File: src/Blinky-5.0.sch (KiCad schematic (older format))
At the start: 7 parts, among them U1 7555

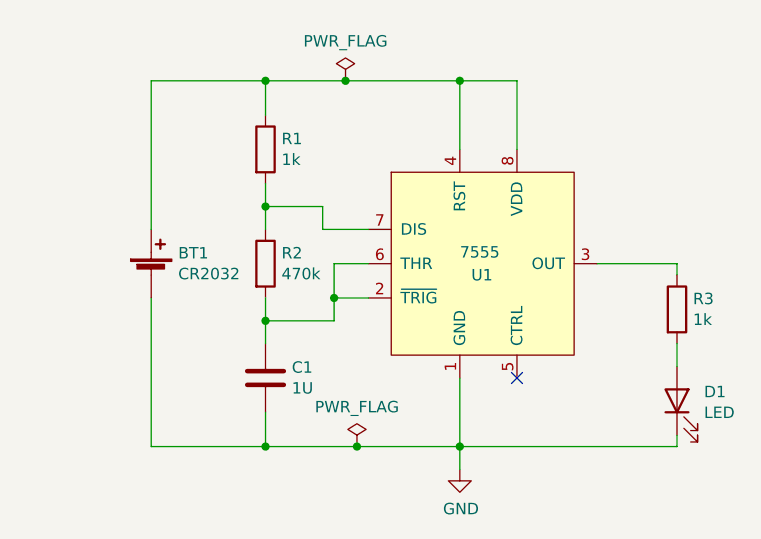
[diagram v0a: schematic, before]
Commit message: Add custom library and additions
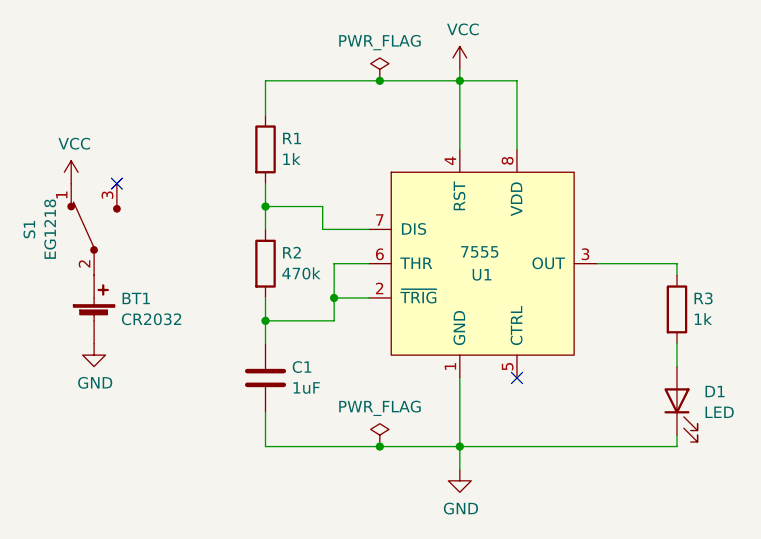
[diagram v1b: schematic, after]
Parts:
- added S1: EG1218, digikey-footprints:Switch_Slide_11.6x4mm_EG1218, symbol dk_Slide-Switches:EG1218
- C1: value 1U -> 1uF
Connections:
- net VCC: now reaches R1.1, U1.4 (RST), U1.8 (VDD)
- net VCC: now also S1.1; no longer BT1.1 (+)
- new net: BT1.1 (+), S1.2
- no-connect marks 1 -> 2
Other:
- moved on the sheet: BT1
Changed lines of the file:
@@
 $EndDescr
-$Comp
-L GTB5:7555 U1
-U 1 1 60908F50
-P 5500 3800
-F 0 "U1" H 5450 3750 50  0000 L CNN
-F 1 "7555" H 5400 3850 50  0000 L CNN
-F 2 "" H 5500 3800 50  0001 C CNN
-F 3 "" H 5500 3800 50  0001 C CNN
-	1    5500 3800
-	1    0    0    -1
-$EndComp
 $Comp
 L Device:R R3
@@
 L Device:Battery_Cell BT1
 U 1 1 6090E03A
-P 4050 3850
-F 0 "BT1" H 4168 3946 50  0000 L CNN
-F 1 "CR2032" H 4168 3855 50  0000 L CNN
-F 2 "" V 4050 3910 50  0001 C CNN
-F 3 "~" V 4050 3910 50  0001 C CNN
-	1    4050 3850
-	1    0    0    -1
-$EndComp
-$Comp
-L power:GND #PWR0101
-U 1 1 6090EEEC
-P 5400 4700
-F 0 "#PWR0101" H 5400 4450 50  0001 C CNN
-F 1 "GND" H 5405 4527 50  0000 C CNN
-F 2 "" H 5400 4700 50  0001 C CNN
-F 3 "" H 5400 4700 50  0001 C CNN
-	1    5400 4700
-	1    0    0    -1
-$EndComp
-Wire Wire Line
-	5650 3000 5650 3300
-Wire Wire Line
-	5400 3300 5400 3000
-Connection ~ 5400 3000
-Wire Wire Line
-	5400 3000 5650 3000
+P 3800 4050
+F 0 "BT1" H 3918 4146 50  0000 L CNN
+F 1 "CR2032" H 3918 4055 50  0000 L CNN
+F 2 "" V 3800 4110 50  0001 C CNN
+F 3 "~" V 3800 4110 50  0001 C CNN
+	1    3800 4050
+	1    0    0    -1
+$EndComp
 $Comp
 L Device:C C1
@@
 P 4550 4300
 F 0 "C1" H 4665 4346 50  0000 L CNN
-F 1 "1U" H 4665 4255 50  0000 L CNN
+F 1 "1uF" H 4665 4255 50  0000 L CNN
 F 2 "" H 4588 4150 50  0001 C CNN
 F 3 "~" H 4550 4300 50  0001 C CNN
@@
 $EndComp
 Wire Wire Line
-	4550 3150 4550 3000
-Connection ~ 4550 3000
-Wire Wire Line
-	4550 3000 4900 3000
-Wire Wire Line
 	4550 3650 4550 3550
 Wire Wire Line
@@
 Wire Wire Line
 	4550 4450 4550 4600
-Connection ~ 4550 4600
+Connection ~ 5400 4600
+Wire Wire Line
+	5400 4600 6350 4600
+Wire Wire Line
+	5400 4600 5400 4300
+NoConn ~ 5650 4300
+$Comp
+L power:VCC #PWR0101
+U 1 1 609267B7
+P 3700 3450
+F 0 "#PWR0101" H 3700 3300 50  0001 C CNN
+F 1 "VCC" H 3715 3623 50  0000 C CNN
+F 2 "" H 3700 3450 50  0001 C CNN
+F 3 "" H 3700 3450 50  0001 C CNN
+	1    3700 3450
+	1    0    0    -1
+$EndComp
+$Comp
+L power:GND #PWR0102
+U 1 1 60927759
+P 3800 4150
+F 0 "#PWR0102" H 3800 3900 50  0001 C CNN
+F 1 "GND" H 3805 3977 50  0000 C CNN
+F 2 "" H 3800 4150 50  0001 C CNN
+F 3 "" H 3800 4150 50  0001 C CNN
+	1    3800 4150
+	1    0    0    -1
+$EndComp
+$Comp
+L power:VCC #PWR0103
+U 1 1 609313FA
+P 5400 2950
+F 0 "#PWR0103" H 5400 2800 50  0001 C CNN
+F 1 "VCC" H 5415 3123 50  0000 C CNN
+F 2 "" H 5400 2950 50  0001 C CNN
+F 3 "" H 5400 2950 50  0001 C CNN
+	1    5400 2950
+	1    0    0    -1
+$EndComp
+$Comp
+L GTB5:7555 U1
+U 1 1 60908F50
+P 5500 3800
+F 0 "U1" H 5450 3750 50  0000 L CNN
+F 1 "7555" H 5400 3850 50  0000 L CNN
+F 2 "" H 5500 3800 50  0001 C CNN
+F 3 "" H 5500 3800 50  0001 C CNN
+	1    5500 3800
+	1    0    0    -1
+$EndComp
+Wire Wire Line
+	5400 3300 5400 3000
+Wire Wire Line
+	4550 3150 4550 3000
+Wire Wire Line
+	4550 3000 5050 3000
+Connection ~ 5400 3000
+Wire Wire Line
+	5650 3300 5650 3000
+Wire Wire Line
+	5650 3000 5400 3000
+Wire Wire Line
+	4550 4600 5050 4600
+Wire Wire Line
+	5400 3000 5400 2950
+$Comp
+L power:GND #PWR0104
+U 1 1 6093A498
+P 5400 4700
+F 0 "#PWR0104" H 5400 4450 50  0001 C CNN
+F 1 "GND" H 5405 4527 50  0000 C CNN
+F 2 "" H 5400 4700 50  0001 C CNN
+F 3 "" H 5400 4700 50  0001 C CNN
+	1    5400 4700
+	1    0    0    -1
+$EndComp
 Wire Wire Line
 	5400 4600 5400 4700
-Wire Wire Line
-	4550 4600 4950 4600
-Connection ~ 5400 4600
-Wire Wire Line
-	5400 4600 6350 4600
-Wire Wire Line
-	5400 4600 5400 4300
-Wire Wire Line
-	4050 3950 4050 4600
-Wire Wire Line
-	4050 4600 4550 4600
-Wire Wire Line
-	4050 3650 4050 3000
-Wire Wire Line
-	4050 3000 4550 3000
 $Comp
 L power:PWR_FLAG #FLG0101
-U 1 1 6091C652
-P 4900 3000
-F 0 "#FLG0101" H 4900 3075 50  0001 C CNN
-F 1 "PWR_FLAG" H 4900 3173 50  0000 C CNN
-F 2 "" H 4900 3000 50  0001 C CNN
-F 3 "~" H 4900 3000 50  0001 C CNN
-	1    4900 3000
-	1    0    0    -1
-$EndComp
-Connection ~ 4900 3000
-Wire Wire Line
-	4900 3000 5400 3000
+U 1 1 6093C855
+P 5050 3000
+F 0 "#FLG0101" H 5050 3075 50  0001 C CNN
+F 1 "PWR_FLAG" H 5050 3173 50  0000 C CNN
+F 2 "" H 5050 3000 50  0001 C CNN
+F 3 "~" H 5050 3000 50  0001 C CNN
+	1    5050 3000
+	1    0    0    -1
+$EndComp
+Connection ~ 5050 3000
+Wire Wire Line
+	5050 3000 5400 3000
 $Comp
 L power:PWR_FLAG #FLG0102
-U 1 1 6091C7F0
-P 4950 4600
-F 0 "#FLG0102" H 4950 4675 50  0001 C CNN
-F 1 "PWR_FLAG" H 4950 4773 50  0000 C CNN
-F 2 "" H 4950 4600 50  0001 C CNN
-F 3 "~" H 4950 4600 50  0001 C CNN
-	1    4950 4600
-	1    0    0    -1
-$EndComp
-Connection ~ 4950 4600
-Wire Wire Line
-	4950 4600 5400 4600
-NoConn ~ 5650 4300
+U 1 1 6093DBDA
+P 5050 4600
+F 0 "#FLG0102" H 5050 4675 50  0001 C CNN
+F 1 "PWR_FLAG" H 5050 4773 50  0000 C CNN
+F 2 "" H 5050 4600 50  0001 C CNN
+F 3 "~" H 5050 4600 50  0001 C CNN
+	1    5050 4600
+	1    0    0    -1
+$EndComp
+Connection ~ 5050 4600
+Wire Wire Line
+	5050 4600 5400 4600
+$Comp
+L dk_Slide-Switches:EG1218 S1
+U 1 1 609476D4
+P 3800 3650
+F 0 "S1" H 3800 3931 50  0000 C CNN
+F 1 "EG1218" H 3800 3840 50  0000 C CNN
+F 2 "digikey-footprints:Switch_Slide_11.6x4mm_EG1218" H 4000 3850 50  0001 L CNN
+F 3 "http://spec_sheets.e-switch.com/specs/P040040.pdf" H 4000 3950 60  0001 L CNN
+F 4 "EG1903-ND" H 4000 4050 60  0001 L CNN "Digi-Key_PN"
+F 5 "EG1218" H 4000 4150 60  0001 L CNN "MPN"
+F 6 "Switches" H 4000 4250 60  0001 L CNN "Category"
+F 7 "Slide Switches" H 4000 4350 60  0001 L CNN "Family"
+F 8 "http://spec_sheets.e-switch.com/specs/P040040.pdf" H 4000 4450 60  0001 L CNN "DK_Datasheet_Link"
+F 9 "/product-detail/en/e-switch/EG1218/EG1903-ND/101726" H 4000 4550 60  0001 L CNN "DK_Detail_Page"
+F 10 "SWITCH SLIDE SPDT 200MA 30V" H 4000 4650 60  0001 L CNN "Description"
+F 11 "E-Switch" H 4000 4750 60  0001 L CNN "Manufacturer"
+F 12 "Active" H 4000 4850 60  0001 L CNN "Status"
+	1    3800 3650
+	0    -1   -1   0
+$EndComp
+NoConn ~ 3900 3450
 $EndSCHEMATC

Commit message: Make some custom footprints and define board layout
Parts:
- removed S1: EG1218, digikey-footprints:Switch_Slide_11.6x4mm_EG1218, symbol dk_Slide-Switches:EG1218
- added SW?: SW_SPDT, src:JS102011SCQN, symbol Switch:SW_SPDT
- BT1: footprint (none) -> src:3034
- C1: footprint (none) -> Capacitor_SMD:C_1206_3216Metric_Pad1.33x1.80mm_HandSolder
- D1: footprint (none) -> LED_SMD:LED_1206_3216Metric_Pad1.42x1.75mm_HandSolder
- R1, R2, R3: footprint (none) -> Resistor_SMD:R_1206_3216Metric_Pad1.30x1.75mm_HandSolder
- U1: footprint (none) -> Package_SO:SOIC-8_3.9x4.9mm_P1.27mm
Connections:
- net VCC: now also SW?.1 (A)
- net at BT1.1 (+): now also SW?.2 (B)
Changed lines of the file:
@@
 F 0 "R3" H 6420 4046 50  0000 L CNN
 F 1 "1k" H 6420 3955 50  0000 L CNN
-F 2 "" V 6280 4000 50  0001 C CNN
+F 2 "Resistor_SMD:R_1206_3216Metric_Pad1.30x1.75mm_HandSolder" V 6280 4000 50  0001 C CNN
 F 3 "~" H 6350 4000 50  0001 C CNN
 	1    6350 4000
@@
 F 0 "D1" V 6389 4282 50  0000 R CNN
 F 1 "LED" V 6298 4282 50  0000 R CNN
-F 2 "" H 6350 4400 50  0001 C CNN
+F 2 "LED_SMD:LED_1206_3216Metric_Pad1.42x1.75mm_HandSolder" H 6350 4400 50  0001 C CNN
 F 3 "~" H 6350 4400 50  0001 C CNN
 	1    6350 4400
@@
 F 0 "BT1" H 3918 4146 50  0000 L CNN
 F 1 "CR2032" H 3918 4055 50  0000 L CNN
-F 2 "" V 3800 4110 50  0001 C CNN
+F 2 "src:3034" V 3800 4110 50  0001 C CNN
 F 3 "~" V 3800 4110 50  0001 C CNN
 	1    3800 4050
@@
 F 0 "C1" H 4665 4346 50  0000 L CNN
 F 1 "1uF" H 4665 4255 50  0000 L CNN
-F 2 "" H 4588 4150 50  0001 C CNN
+F 2 "Capacitor_SMD:C_1206_3216Metric_Pad1.33x1.80mm_HandSolder" H 4588 4150 50  0001 C CNN
 F 3 "~" H 4550 4300 50  0001 C CNN
 	1    4550 4300
@@
 F 0 "R2" H 4620 3846 50  0000 L CNN
 F 1 "470k" H 4620 3755 50  0000 L CNN
-F 2 "" V 4480 3800 50  0001 C CNN
+F 2 "Resistor_SMD:R_1206_3216Metric_Pad1.30x1.75mm_HandSolder" V 4480 3800 50  0001 C CNN
 F 3 "~" H 4550 3800 50  0001 C CNN
 	1    4550 3800
@@
 F 0 "R1" H 4620 3346 50  0000 L CNN
 F 1 "1k" H 4620 3255 50  0000 L CNN
-F 2 "" V 4480 3300 50  0001 C CNN
+F 2 "Resistor_SMD:R_1206_3216Metric_Pad1.30x1.75mm_HandSolder" V 4480 3300 50  0001 C CNN
 F 3 "~" H 4550 3300 50  0001 C CNN
 	1    4550 3300
@@
 $EndComp
 $Comp
-L power:VCC #PWR0103
+L power:VCC #PWR0101
 U 1 1 609313FA
 P 5400 2950
-F 0 "#PWR0103" H 5400 2800 50  0001 C CNN
+F 0 "#PWR0101" H 5400 2800 50  0001 C CNN
 F 1 "VCC" H 5415 3123 50  0000 C CNN
 F 2 "" H 5400 2950 50  0001 C CNN
@@
 F 0 "U1" H 5450 3750 50  0000 L CNN
 F 1 "7555" H 5400 3850 50  0000 L CNN
-F 2 "" H 5500 3800 50  0001 C CNN
+F 2 "Package_SO:SOIC-8_3.9x4.9mm_P1.27mm" H 5500 3800 50  0001 C CNN
 F 3 "" H 5500 3800 50  0001 C CNN
 	1    5500 3800
@@
 	5400 3000 5400 2950
 $Comp
-L power:GND #PWR0104
+L power:GND #PWR0102
 U 1 1 6093A498
 P 5400 4700
-F 0 "#PWR0104" H 5400 4450 50  0001 C CNN
+F 0 "#PWR0102" H 5400 4450 50  0001 C CNN
 F 1 "GND" H 5405 4527 50  0000 C CNN
 F 2 "" H 5400 4700 50  0001 C CNN
@@
 	5050 4600 5400 4600
 $Comp
-L dk_Slide-Switches:EG1218 S1
-U 1 1 609476D4
+L Switch:SW_SPDT SW?
+U 1 1 6096FD5C
 P 3800 3650
-F 0 "S1" H 3800 3931 50  0000 C CNN
-F 1 "EG1218" H 3800 3840 50  0000 C CNN
-F 2 "digikey-footprints:Switch_Slide_11.6x4mm_EG1218" H 4000 3850 50  0001 L CNN
-F 3 "http://spec_sheets.e-switch.com/specs/P040040.pdf" H 4000 3950 60  0001 L CNN
-F 4 "EG1903-ND" H 4000 4050 60  0001 L CNN "Digi-Key_PN"
-F 5 "EG1218" H 4000 4150 60  0001 L CNN "MPN"
-F 6 "Switches" H 4000 4250 60  0001 L CNN "Category"
-F 7 "Slide Switches" H 4000 4350 60  0001 L CNN "Family"
-F 8 "http://spec_sheets.e-switch.com/specs/P040040.pdf" H 4000 4450 60  0001 L CNN "DK_Datasheet_Link"
-F 9 "/product-detail/en/e-switch/EG1218/EG1903-ND/101726" H 4000 4550 60  0001 L CNN "DK_Detail_Page"
-F 10 "SWITCH SLIDE SPDT 200MA 30V" H 4000 4650 60  0001 L CNN "Description"
-F 11 "E-Switch" H 4000 4750 60  0001 L CNN "Manufacturer"
-F 12 "Active" H 4000 4850 60  0001 L CNN "Status"
+F 0 "SW?" V 3846 3462 50  0000 R CNN
+F 1 "SW_SPDT" V 3755 3462 50  0000 R CNN
+F 2 "src:JS102011SCQN" H 3800 3650 50  0001 C CNN
+F 3 "~" H 3800 3650 50  0001 C CNN
 	1    3800 3650
 	0    -1   -1   0

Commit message: Add some changes and finish layout
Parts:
- R3: value 1k -> 150
- gave numbers to parts that had none: 1
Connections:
- net VCC renamed VDD
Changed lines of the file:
@@
 P 6350 4000
 F 0 "R3" H 6420 4046 50  0000 L CNN
-F 1 "1k" H 6420 3955 50  0000 L CNN
+F 1 "150" H 6420 3955 50  0000 L CNN
 F 2 "Resistor_SMD:R_1206_3216Metric_Pad1.30x1.75mm_HandSolder" V 6280 4000 50  0001 C CNN
 F 3 "~" H 6350 4000 50  0001 C CNN
@@
 NoConn ~ 5650 4300
 $Comp
-L power:VCC #PWR0101
-U 1 1 609267B7
-P 3700 3450
-F 0 "#PWR0101" H 3700 3300 50  0001 C CNN
-F 1 "VCC" H 3715 3623 50  0000 C CNN
-F 2 "" H 3700 3450 50  0001 C CNN
-F 3 "" H 3700 3450 50  0001 C CNN
-	1    3700 3450
-	1    0    0    -1
-$EndComp
-$Comp
-L power:GND #PWR0102
-U 1 1 60927759
-P 3800 4150
-F 0 "#PWR0102" H 3800 3900 50  0001 C CNN
-F 1 "GND" H 3805 3977 50  0000 C CNN
-F 2 "" H 3800 4150 50  0001 C CNN
-F 3 "" H 3800 4150 50  0001 C CNN
-	1    3800 4150
-	1    0    0    -1
-$EndComp
-$Comp
-L power:VCC #PWR0101
-U 1 1 609313FA
-P 5400 2950
-F 0 "#PWR0101" H 5400 2800 50  0001 C CNN
-F 1 "VCC" H 5415 3123 50  0000 C CNN
-F 2 "" H 5400 2950 50  0001 C CNN
-F 3 "" H 5400 2950 50  0001 C CNN
-	1    5400 2950
-	1    0    0    -1
-$EndComp
-$Comp
 L GTB5:7555 U1
 U 1 1 60908F50
@@
 Wire Wire Line
 	4550 3150 4550 3000
-Wire Wire Line
-	4550 3000 5050 3000
 Connection ~ 5400 3000
 Wire Wire Line
@@
 	5650 3000 5400 3000
 Wire Wire Line
-	4550 4600 5050 4600
-Wire Wire Line
 	5400 3000 5400 2950
 $Comp
-L power:GND #PWR0102
-U 1 1 6093A498
-P 5400 4700
-F 0 "#PWR0102" H 5400 4450 50  0001 C CNN
-F 1 "GND" H 5405 4527 50  0000 C CNN
-F 2 "" H 5400 4700 50  0001 C CNN
-F 3 "" H 5400 4700 50  0001 C CNN
-	1    5400 4700
-	1    0    0    -1
-$EndComp
-Wire Wire Line
-	5400 4600 5400 4700
-$Comp
-L power:PWR_FLAG #FLG0101
-U 1 1 6093C855
-P 5050 3000
-F 0 "#FLG0101" H 5050 3075 50  0001 C CNN
-F 1 "PWR_FLAG" H 5050 3173 50  0000 C CNN
-F 2 "" H 5050 3000 50  0001 C CNN
-F 3 "~" H 5050 3000 50  0001 C CNN
-	1    5050 3000
-	1    0    0    -1
-$EndComp
-Connection ~ 5050 3000
-Wire Wire Line
-	5050 3000 5400 3000
-$Comp
-L power:PWR_FLAG #FLG0102
-U 1 1 6093DBDA
-P 5050 4600
-F 0 "#FLG0102" H 5050 4675 50  0001 C CNN
-F 1 "PWR_FLAG" H 5050 4773 50  0000 C CNN
-F 2 "" H 5050 4600 50  0001 C CNN
-F 3 "~" H 5050 4600 50  0001 C CNN
-	1    5050 4600
-	1    0    0    -1
-$EndComp
-Connection ~ 5050 4600
-Wire Wire Line
-	5050 4600 5400 4600
-$Comp
-L Switch:SW_SPDT SW?
+L Switch:SW_SPDT SW1
 U 1 1 6096FD5C
 P 3800 3650
-F 0 "SW?" V 3846 3462 50  0000 R CNN
+F 0 "SW1" V 3846 3462 50  0000 R CNN
 F 1 "SW_SPDT" V 3755 3462 50  0000 R CNN
 F 2 "src:JS102011SCQN" H 3800 3650 50  0001 C CNN
@@
 $EndComp
 NoConn ~ 3900 3450
+Wire Wire Line
+	4550 3000 5000 3000
+Wire Wire Line
+	4550 4600 5050 4600
+$Comp
+L power:GND #PWR0103
+U 1 1 60A652DB
+P 3800 4150
+F 0 "#PWR0103" H 3800 3900 50  0001 C CNN
+F 1 "GND" H 3805 3977 50  0000 C CNN
+F 2 "" H 3800 4150 50  0001 C CNN
+F 3 "" H 3800 4150 50  0001 C CNN
+	1    3800 4150
+	1    0    0    -1
+$EndComp
+$Comp
+L power:GND #PWR0104
+U 1 1 60A6572D
+P 5400 4600
+F 0 "#PWR0104" H 5400 4350 50  0001 C CNN
+F 1 "GND" H 5405 4427 50  0000 C CNN
+F 2 "" H 5400 4600 50  0001 C CNN
+F 3 "" H 5400 4600 50  0001 C CNN
+	1    5400 4600
+	1    0    0    -1
+$EndComp
+$Comp
+L power:PWR_FLAG #FLG0101
+U 1 1 60A6BA92
+P 5050 4600
+F 0 "#FLG0101" H 5050 4675 50  0001 C CNN
+F 1 "PWR_FLAG" H 5050 4773 50  0000 C CNN
+F 2 "" H 5050 4600 50  0001 C CNN
+F 3 "~" H 5050 4600 50  0001 C CNN
+	1    5050 4600
+	1    0    0    -1
+$EndComp
+Connection ~ 5050 4600
+Wire Wire Line
+	5050 4600 5400 4600
+$Comp
+L power:PWR_FLAG #FLG0102
+U 1 1 60A6BEB8
+P 5000 3000
+F 0 "#FLG0102" H 5000 3075 50  0001 C CNN
+F 1 "PWR_FLAG" H 5000 3173 50  0000 C CNN
+F 2 "" H 5000 3000 50  0001 C CNN
+F 3 "~" H 5000 3000 50  0001 C CNN
+	1    5000 3000
+	1    0    0    -1
+$EndComp
+Connection ~ 5000 3000
+Wire Wire Line
+	5000 3000 5400 3000
+$Comp
+L power:VDD #PWR?
+U 1 1 60A6D897
+P 3700 3450
+F 0 "#PWR?" H 3700 3300 50  0001 C CNN
+F 1 "VDD" H 3715 3623 50  0000 C CNN
+F 2 "" H 3700 3450 50  0001 C CNN
+F 3 "" H 3700 3450 50  0001 C CNN
+	1    3700 3450
+	1    0    0    -1
+$EndComp
+$Comp
+L power:VDD #PWR?
+U 1 1 60A6E50B
+P 5400 2950
+F 0 "#PWR?" H 5400 2800 50  0001 C CNN
+F 1 "VDD" H 5415 3123 50  0000 C CNN
+F 2 "" H 5400 2950 50  0001 C CNN
+F 3 "" H 5400 2950 50  0001 C CNN
+	1    5400 2950
+	1    0    0    -1
+$EndComp
 $EndSCHEMATC
